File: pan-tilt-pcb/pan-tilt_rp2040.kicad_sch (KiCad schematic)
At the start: 26 parts, among them U1 RP2040, U2 W25Q32JVSS, Y1 ABM8-272-T3

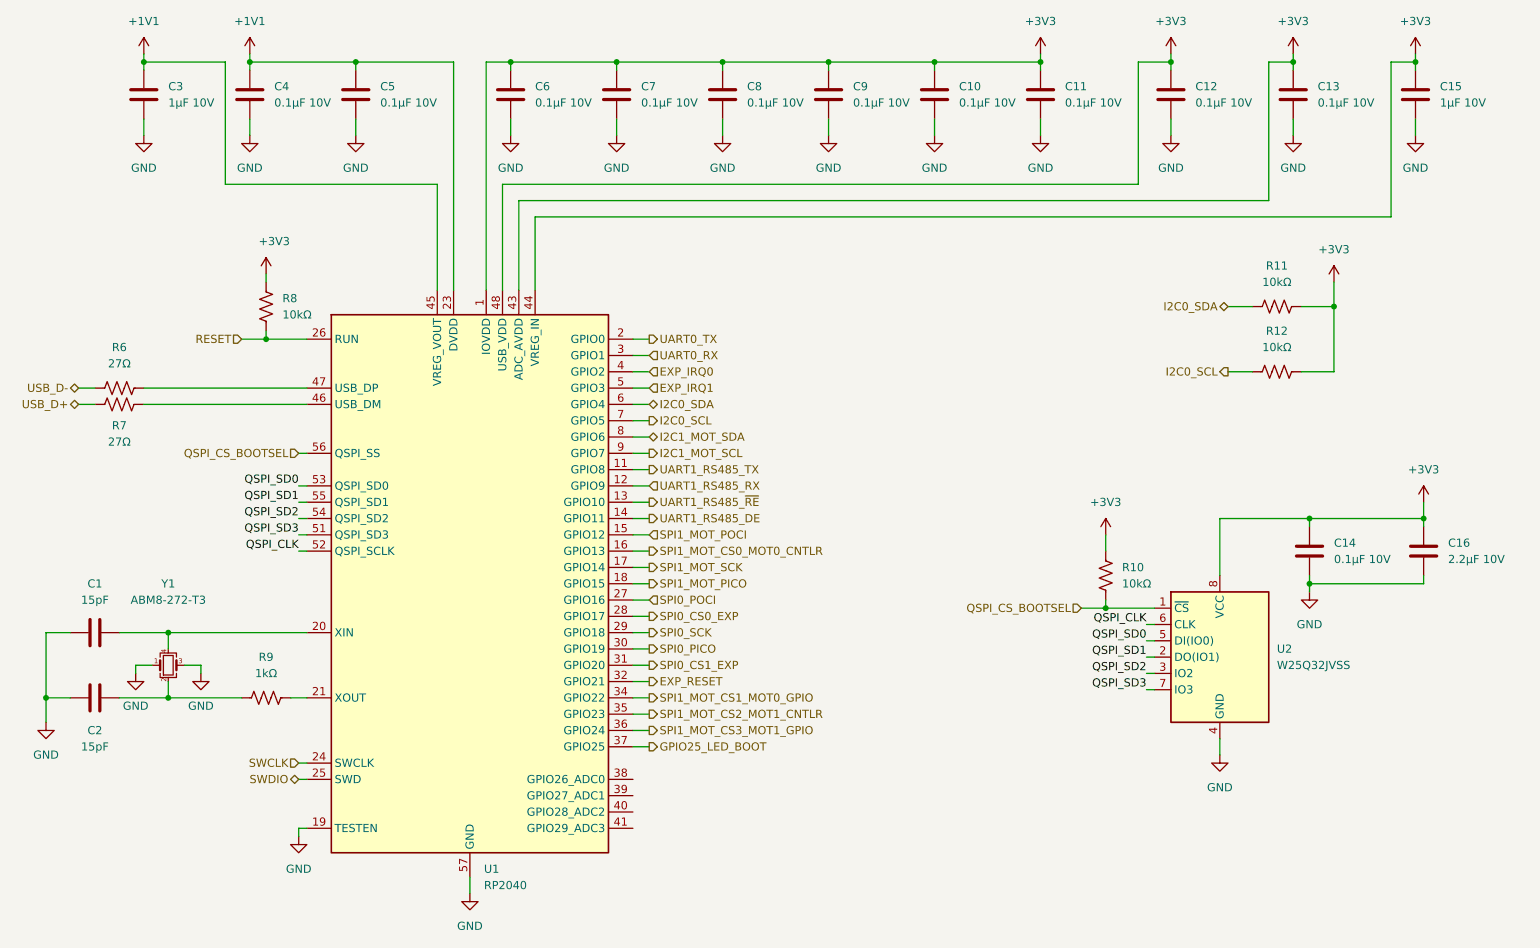
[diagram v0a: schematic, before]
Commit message: fix missing pieces, incorporate review feedback
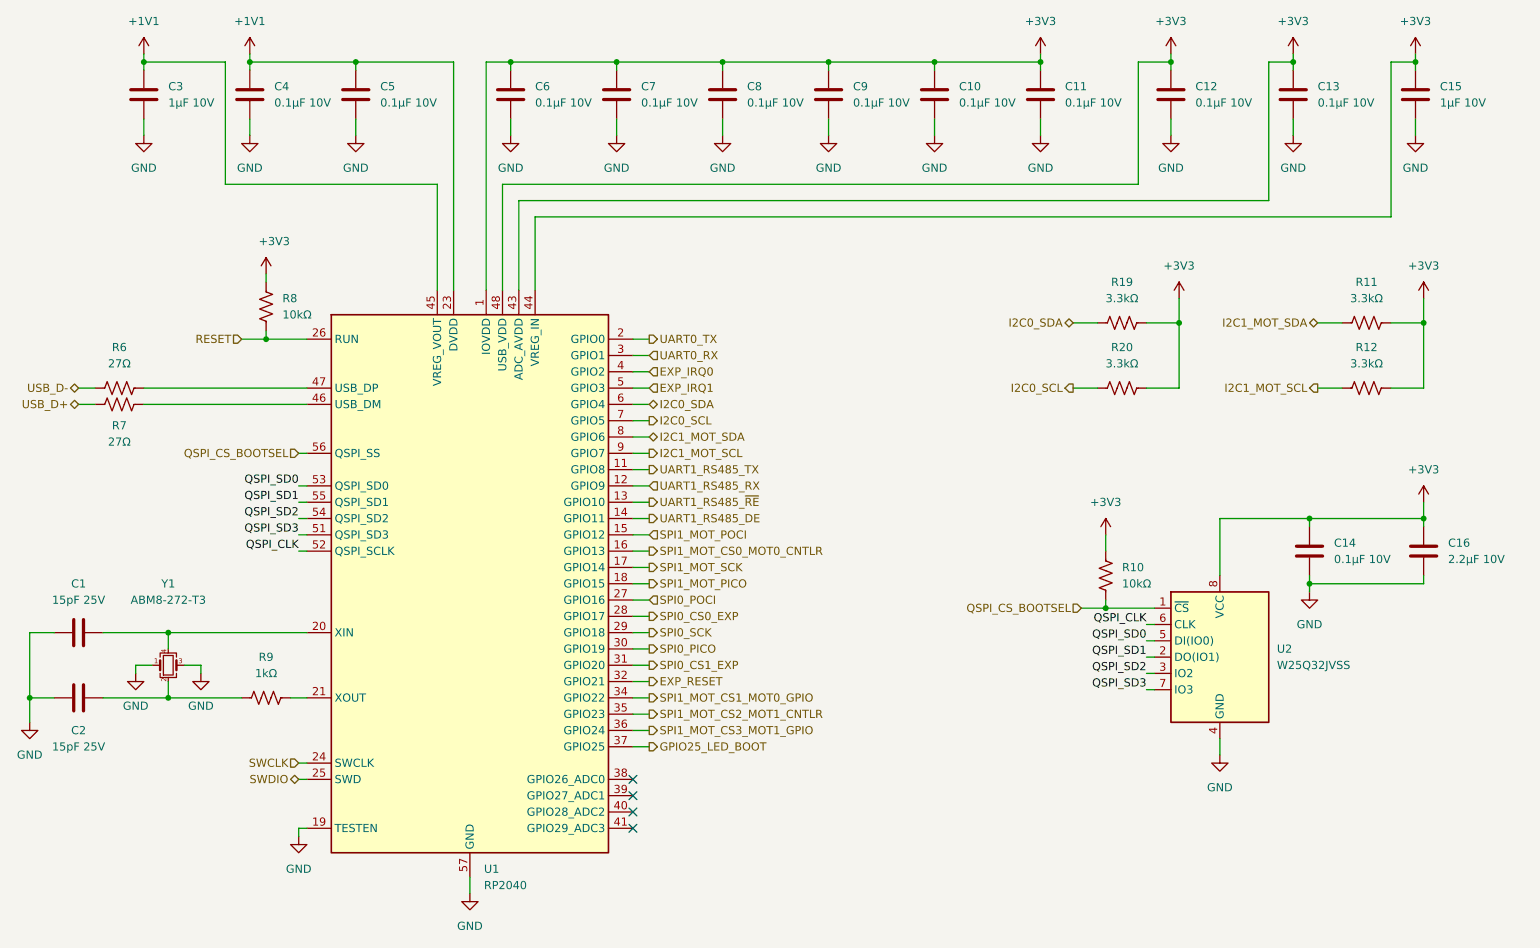
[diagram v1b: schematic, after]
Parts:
- added R19, R20: 3.3kΩ, symbol Device:R_US
- C1, C2: value 15pF -> 15pF 25V
- R11, R12: value 10kΩ -> 3.3kΩ
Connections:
- net +3V3: now also R19.2, R20.2
- net I2C0_SCL: now also R20.1; no longer R12.1
- net I2C0_SDA: now also R19.1; no longer R11.1
- net I2C1_MOT_SCL: now also R12.1
- net I2C1_MOT_SDA: now also R11.1
- no-connect marks 0 -> 4
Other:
- moved on the sheet: C1, C2, R11, R12
